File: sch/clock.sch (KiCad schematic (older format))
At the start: 2 parts, among them U1 SI570, U2 74ACT74

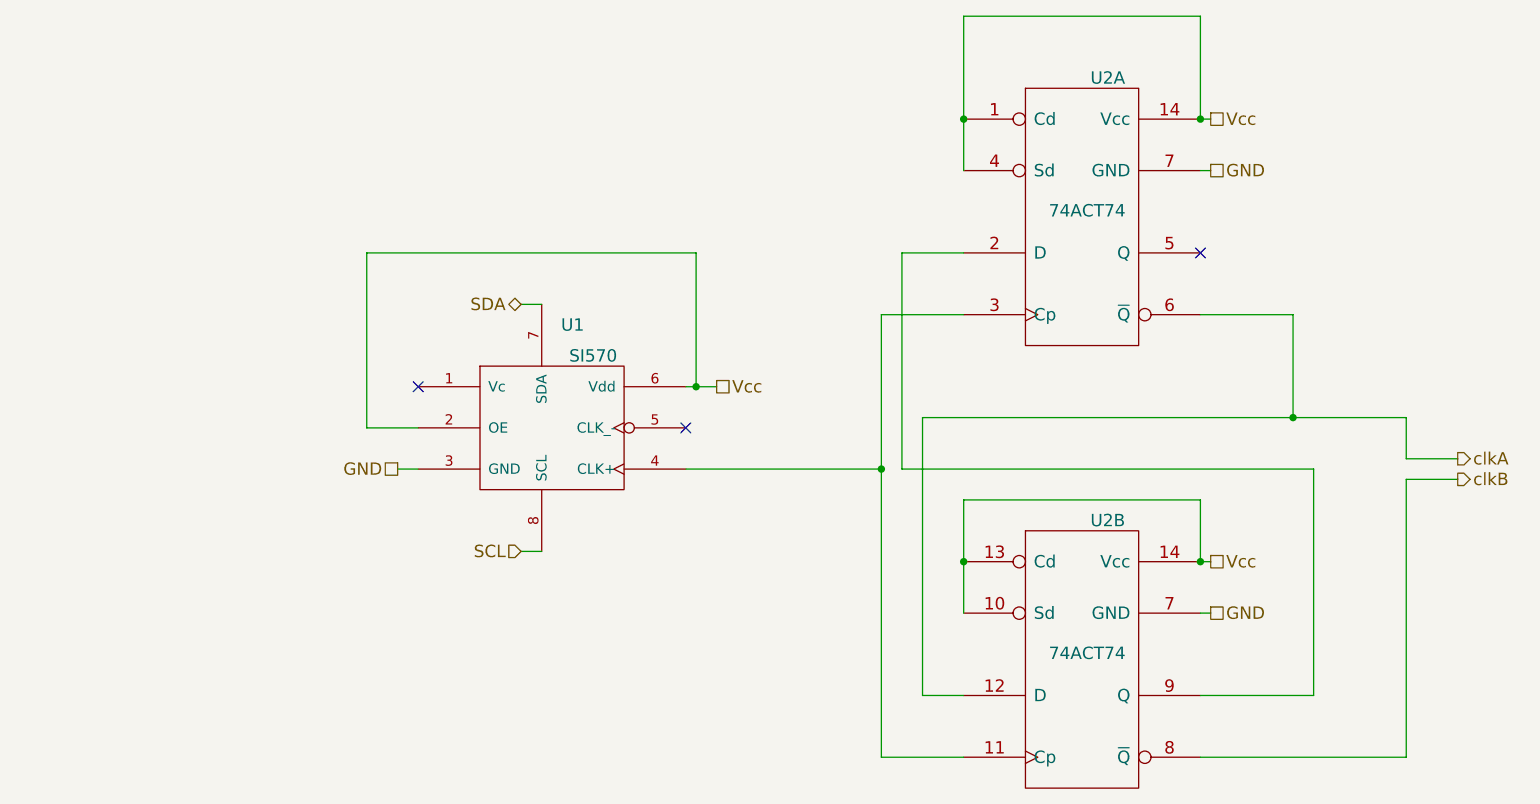
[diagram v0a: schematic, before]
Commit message: add FIN1002 buffer for LVDS variant of Si570
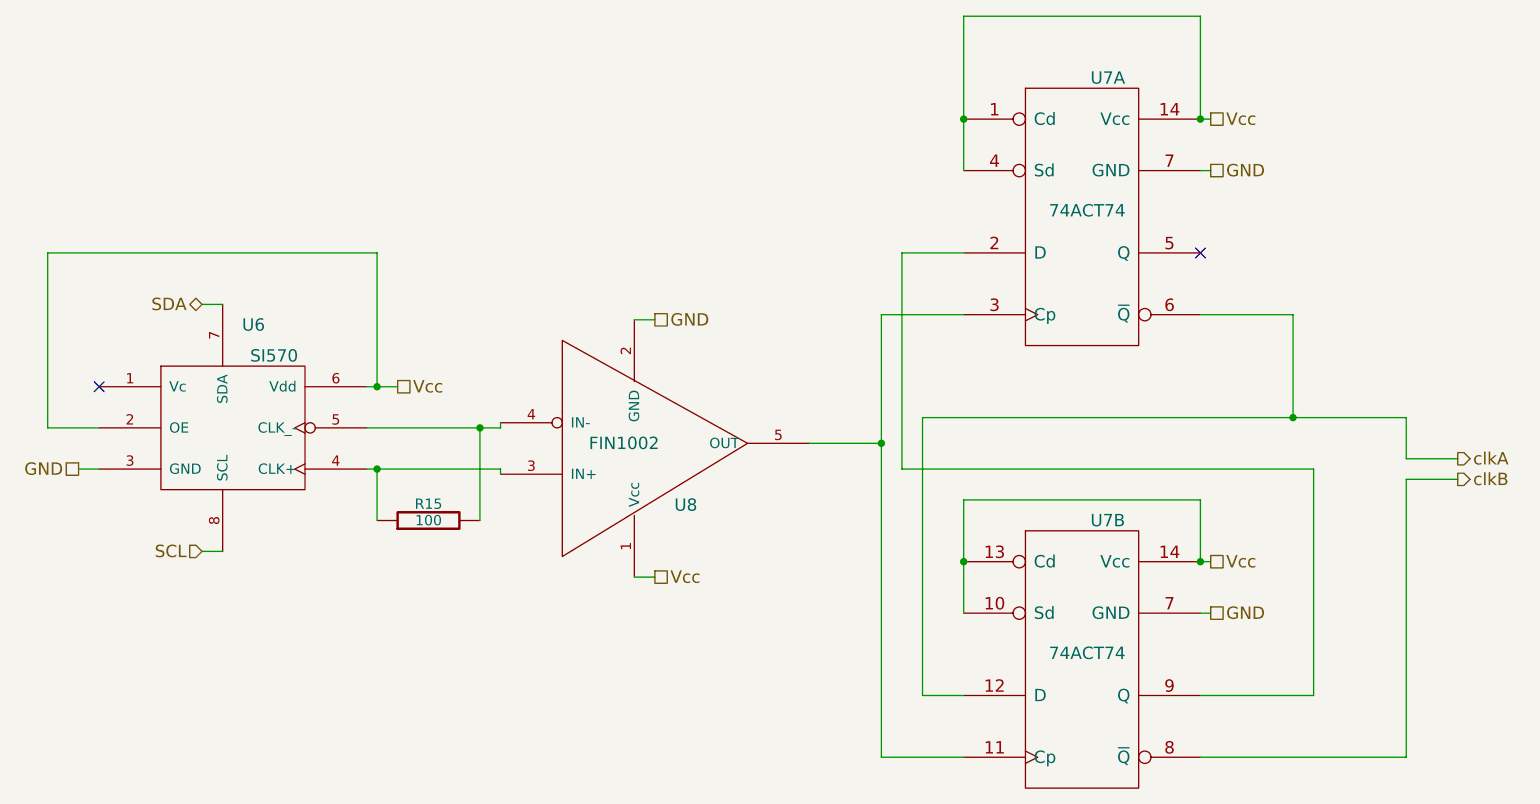
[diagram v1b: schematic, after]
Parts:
- added R15: 100, symbol R
- added U8: FIN1002, symbol FIN1002
- renumbered U1 to U6, U2 to U7
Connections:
- net GND: now also U8.2 (GND)
- net Vcc: now also U8.1 (Vcc)
- net at U7.11 (Cp), U7.3 (Cp): now also U8.5 (OUT); no longer U6.4 (CLK+)
- net at U6.5 (CLK_-): now also R15.2, U8.4 (IN-)
- new net: R15.1, U6.4 (CLK+), U8.3 (IN+)
- no-connect marks 3 -> 2
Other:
- moved on the sheet: U6
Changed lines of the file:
@@
-EESchema Schematic File Version 2  date so 30 črv 00:27:22 2012
+EESchema Schematic File Version 2  date so 30 črv 11:50:59 2012
 LIBS:power
 LIBS:device
@@
 LIBS:ms-audio
 LIBS:ms-conn
+LIBS:ms-ti
+LIBS:hf-sampling-trx-cache
 EELAYER 25  0
 EELAYER END
 $Descr A4 11693 8268
 encoding utf-8
-Sheet 4 4
+Sheet 4 5
 Title ""
-Date "29 jun 2012"
+Date "30 jun 2012"
 Rev ""
 Comp ""
@@
 $EndDescr
 $Comp
-L SI570 U1
+L SI570 U6
 U 1 1 4FEDF8E1
-P 5650 3250
-F 0 "U1" H 5800 3750 60  0000 C CNN
-F 1 "SI570" H 5900 3600 60  0000 C CNN
-	1    5650 3250
+P 4100 3250
+F 0 "U6" H 4250 3750 60  0000 C CNN
+F 1 "SI570" H 4350 3600 60  0000 C CNN
+	1    4100 3250
 	1    0    0    -1
 $EndComp
-Text HLabel 5550 2650 0    60   BiDi ~ 0
+Text HLabel 4000 2650 0    60   BiDi ~ 0
 SDA
-Text HLabel 5550 3850 0    60   Input ~ 0
+Text HLabel 4000 3850 0    60   Input ~ 0
 SCL
-Text HLabel 4950 3450 0    60   UnSpc ~ 0
-GND
-NoConn ~ 5050 3050
-NoConn ~ 6350 3250
-Text HLabel 6500 3050 2    60   UnSpc ~ 0
+Text HLabel 3400 3450 0    60   UnSpc ~ 0
+GND
+NoConn ~ 3500 3050
+Text HLabel 4950 3050 2    60   UnSpc ~ 0
 Vcc
 Text HLabel 10100 3400 2    60   Output ~ 0
@@
 clkB
 $Comp
-L 74ACT74 U2
+L 74ACT74 U7
 U 1 1 4FEE0440
 P 8250 2200
-F 0 "U2" H 8400 2850 60  0000 C CNN
+F 0 "U7" H 8400 2850 60  0000 C CNN
 F 1 "74ACT74" H 8300 2205 60  0000 C CNN
 	1    8250 2200
@@
 $EndComp
 $Comp
-L 74ACT74 U2
+L 74ACT74 U7
 U 2 1 4FEE044F
 P 8250 4350
-F 0 "U2" H 8400 5000 60  0000 C CNN
+F 0 "U7" H 8400 5000 60  0000 C CNN
 F 1 "74ACT74" H 8300 4355 60  0000 C CNN
 	2    8250 4350
@@
 GND
 NoConn ~ 8850 2400
-Wire Wire Line
-	5550 2650 5650 2650
-Wire Wire Line
-	5550 3850 5650 3850
-Wire Wire Line
-	6350 3050 6500 3050
-Wire Wire Line
-	4950 3450 5050 3450
-Wire Wire Line
-	5050 3250 4800 3250
-Wire Wire Line
-	6350 3450 7300 3450
+$Comp
+L FIN1002 U8
+U 1 1 4FEECB2F
+P 6050 3325
+F 0 "U8" H 6350 3625 60  0000 C CNN
+F 1 "FIN1002" H 6050 3325 60  0000 C CNN
+	1    6050 3325
+	1    0    0    1
+$EndComp
+Text HLabel 6200 3975 2    60   UnSpc ~ 0
+Vcc
+Text HLabel 6200 2725 2    60   UnSpc ~ 0
+GND
+$Comp
+L R R15
+U 1 1 4FEECE1E
+P 5100 3700
+F 0 "R15" V 5180 3700 50  0000 C CNN
+F 1 "100" V 5100 3700 50  0000 C CNN
+	1    5100 3700
+	0    -1   -1   0
+$EndComp
+Wire Wire Line
+	4000 2650 4100 2650
+Wire Wire Line
+	4000 3850 4100 3850
+Wire Wire Line
+	4800 3050 4950 3050
+Wire Wire Line
+	3400 3450 3500 3450
+Wire Wire Line
+	3500 3250 3250 3250
 Wire Wire Line
 	7300 2700 7300 4850
@@
 Wire Wire Line
 	7300 4850 7700 4850
-Connection ~ 7300 3450
 Wire Wire Line
 	7700 4550 7500 4550
@@
 Connection ~ 8850 3900
 Wire Wire Line
-	4800 3250 4800 2400
-Wire Wire Line
-	4800 2400 6400 2400
-Wire Wire Line
-	6400 2400 6400 3050
-Connection ~ 6400 3050
+	3250 3250 3250 2400
+Wire Wire Line
+	3250 2400 4850 2400
+Wire Wire Line
+	4850 2400 4850 3050
+Connection ~ 4850 3050
+Wire Wire Line
+	4800 3250 5450 3250
+Wire Wire Line
+	5450 3250 5450 3225
+Wire Wire Line
+	4800 3450 5450 3450
+Wire Wire Line
+	5450 3450 5450 3475
+Wire Wire Line
+	6950 3325 7300 3325
+Connection ~ 7300 3325
+Wire Wire Line
+	6100 2725 6200 2725
+Wire Wire Line
+	6100 3975 6200 3975
+Wire Wire Line
+	5350 3700 5350 3250
+Connection ~ 5350 3250
+Wire Wire Line
+	4850 3700 4850 3450
+Connection ~ 4850 3450
 $EndSCHEMATC
